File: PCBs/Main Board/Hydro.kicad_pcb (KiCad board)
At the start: 2 copper layers, 34 parts, among them J1 S2P-VHLFSN, J2 S2P-VHLFSN, J3 S2P-VHLFSN, J4 S2P-VHLFSN, J5 S2P-VHLFSN, J6 436500301, J7 436500301, J8 43650-0401, J9 S2P-VHLFSN, Q1 FQP30N06L, Q2 FQP30N06L, Q3 FQP30N06L, Q4 FQP30N06L, Q5 FQP30N06L, SW1 1825910-6, U1 19p_Header, U2 ESP32_WROOM-32U, U3 19p_Header, U4 173010378

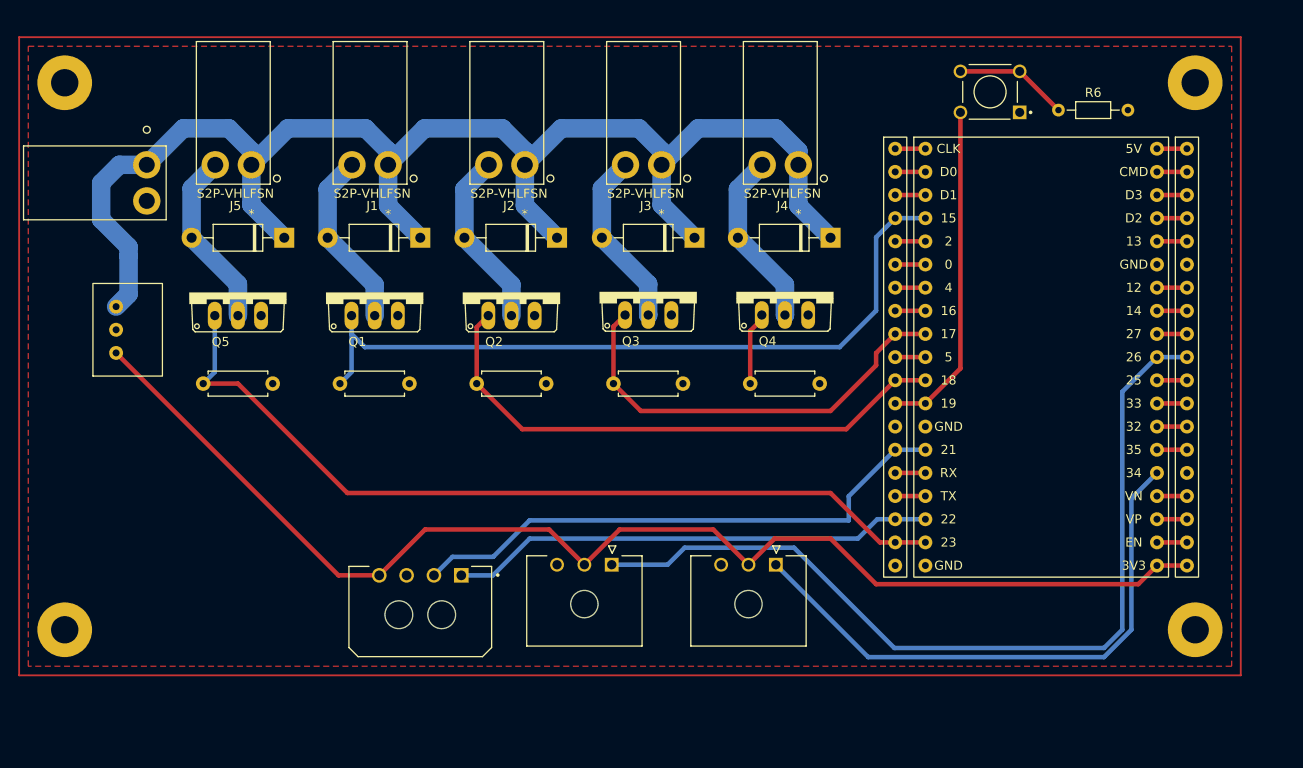
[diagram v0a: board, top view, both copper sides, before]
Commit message: Remove steppers, add OLED
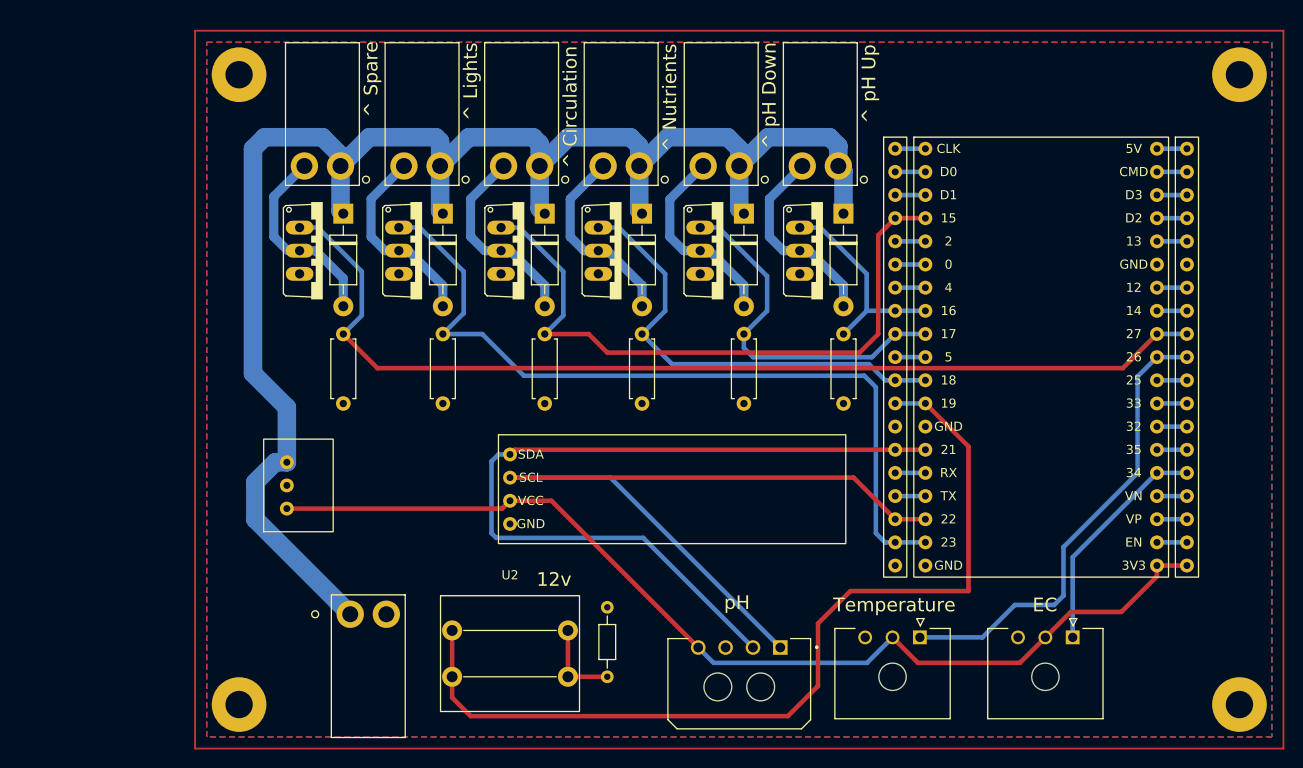
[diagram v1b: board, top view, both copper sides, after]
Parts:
- removed SW1: 1825910-6, SnapEDA Library:SW_1825910-6-4
- added D6: 1N4007, Diode_THT:D_DO-41_SOD81_P10.16mm_Horizontal, F.Cu at (130.6, 54.4)
- added J6: S2P-VHLFSN, Hydro:S2P-VHLFSN, F.Cu at (130.2, 49.1)
- added Q6: FQP30N06L, SnapEDA Library:TO220V, F.Cu at (128.3, 58.4)
- added R6: 1k, Resistor_THT:R_Axial_DIN0207_L6.3mm_D2.5mm_P7.62mm_Horizontal, F.Cu at (130.6, 67.6)
- added U2: Tactile_Button, Hydro:Tactile_Button, F.Cu at (148.8, 102.6)
- added U5: 0.91_OLED, Hydro:0.91 OLED, F.Cu at (166.6, 84.6)
- moved R7 79.5 mm to (159.5, 105.2), turned to 90 degrees
- moved J10 54.1 mm to (131.3, 98.3), turned to 0 degrees
- moved J9 35.9 mm to (174.0, 105.9)
- moved J8 34.7 mm to (193.8, 100.8)
- moved J7 33.5 mm to (210.6, 100.8)
- moved R5 26.8 mm to (141.5, 67.6), turned to -90 degrees
- moved U6 25.3 mm to (129.4, 79.1)
- moved R1 23.1 mm to (152.7, 67.6), turned to -90 degrees
- moved H2 20.8 mm to (119.1, 108.2)
- moved Q5 20.7 mm to (139.2, 58.4), turned to -90 degrees
- moved J5 20.7 mm to (141.2, 49.1)
- moved H3 19.1 mm to (119.1, 39.1)
- moved R2 18.9 mm to (163.3, 67.6), turned to -90 degrees
- moved D5 17.6 mm to (141.5, 54.4), turned to -90 degrees
- moved Q1 17.0 mm to (150.4, 58.4), turned to -90 degrees
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- renumbered J9 to J10, J6 to J7, J7 to J8, J8 to J9, R6 to R7, U2 to U3, U3 to U4, U4 to U6
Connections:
- net Net-(U2-Pad28) renamed Spare
- net pH_rx renamed SCL
- net pH_tx renamed SDA
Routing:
- net Spare: track 3.29 -> 112.2 mm
- net Net-(U1-Pad12): track 36.8 -> 100.4 mm
- net tempSignal: track 96.9 -> 51.4 mm
- net ec_A: track 62.8 -> 25.2 mm
- net SCL: track 53.5 -> 84.8 mm
- net SDA: track 61.2 -> 89.9 mm
- net 3V3: track 138.6 -> 113.9 mm
- net Net-(D6-Pad2): track 0.00 -> 21.7 mm
- net 12v: track 161.1 -> 178.0 mm
- net pHUp: track 11.2 -> 23.5 mm
- net Nutrients: track 61.5 -> 50.3 mm
- net Circulate: track 82.1 -> 71.6 mm
- net pHDown: track 47.8 -> 39.9 mm
- net Lights: track 94.4 -> 88.7 mm
- net Net-(D3-Pad2): track 19.7 -> 23.2 mm
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- added copper zone on B.Cu, net GND
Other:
- board text added: "12v"
- board text added: "EC"
- board text added: "Temperature"
- board text added: "^ Circulation"
- board text added: "^ Lights"
- board text added: "^ Nutrients"
- board text added: "^ Spare"
- board text added: "^ pH Down"
- board text added: "^ pH Up"
- board text added: "pH"

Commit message: update pcb
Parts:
- moved U6 0.86 mm to (129.9, 78.4)
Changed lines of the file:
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@@
+      (effects (font (size 1 1) (thickness 0.15)))
+    )
+    (fp_text user "SDA" (at -15.494 -3.81 unlocked) (layer "F.SilkS")
+      (effects (font (size 1 1) (thickness 0.15)))
+    )
+    (fp_text user "SCL" (at -15.494 -1.27 unlocked) (layer "F.SilkS")
+      (effects (font (size 1 1) (thickness 0.15)))
+    )
+    (fp_text user "GND" (at -15.494 3.81 unlocked) (layer "F.SilkS")
       (effects (font (size 1 1) (thickness 0.15)))
     )
@@
       (effects (font (size 1 1) (thickness 0.15)))
     )
-    (fp_text user "SCL" (at -15.494 -1.27 unlocked) (layer "F.SilkS")
-      (effects (font (size 1 1) (thickness 0.15)))
-    )
-    (fp_text user "GND" (at -15.494 3.81 unlocked) (layer "F.SilkS")
-      (effects (font (size 1 1) (thickness 0.15)))
-    )
-    (fp_text user "SDA" (at -15.494 -3.81 unlocked) (layer "F.SilkS")
-      (effects (font (size 1 1) (thickness 0.15)))
-    )
     (fp_text user "${REFERENCE}" (at 0 -7.62 unlocked) (layer "F.Fab") hide
       (effects (font (size 1 1) (thickness 0.15)))
     )
     (fp_rect (start -19.05 -5.969) (end 19.05 5.969) (layer "F.SilkS") (width 0.12) (fill none))
-    (pad "1" thru_hole circle (at -17.78 -3.81) (size 1.524 1.524) (drill 0.762) (layers *.Cu *.Mask)
+    (pad "1" thru_hole circle (at -17.78 -3.81) (size 2 2) (drill 0.9) (layers *.Cu *.Mask)
       (net 29 "SDA") (pinfunction "SDA") (pintype "input"))
-    (pad "2" thru_hole circle (at -17.78 -1.27) (size 1.524 1.524) (drill 0.762) (layers *.Cu *.Mask)
+    (pad "2" thru_hole circle (at -17.78 -1.27) (size 2 2) (drill 0.9) (layers *.Cu *.Mask)
       (net 28 "SCL") (pinfunction "SCL") (pintype "input"))
-    (pad "3" thru_hole circle (at -17.78 1.27) (size 1.524 1.524) (drill 0.762) (layers *.Cu *.Mask)
+    (pad "3" thru_hole circle (at -17.78 1.27) (size 2 2) (drill 0.9) (layers *.Cu *.Mask)
       (net 23 "3V3") (pinfunction "VCC") (pintype "input"))
-    (pad "4" thru_hole circle (at -17.78 3.81) (size 1.524 1.524) (drill 0.762) (layers *.Cu *.Mask)
+    (pad "4" thru_hole circle (at -17.78 3.81) (size 2 2) (drill 0.9) (layers *.Cu *.Mask)
       (net 7 "GND") (pinfunction "GND") (pintype "input"))
   )
   (footprint "Hydro:173010378" (layer "F.Cu")
-    (at 129.445 79.089 -90)
+    (at 129.918 78.369 -90)
     (property "Sheetfile" "File: PowerSupply.kicad_sch")
     (property "Sheetname" "Power Supply")
@@
       (effects (font (size 1 1) (thickness 0.15)))
     )
-    (fp_rect (start 10.16 7.62) (end 0 0) (layer "F.SilkS") (width 0.12) (fill none))
-    (pad "1" thru_hole circle (at 2.54 5.08 90) (size 1.524 1.524) (drill 0.762) (layers *.Cu *.Mask)
+    (fp_rect (start 11.6 7.55) (end 0 0) (layer "F.SilkS") (width 0.12) (fill none))
+    (pad "1" thru_hole circle (at 3.26 5.4 90) (size 1.524 1.524) (drill 0.762) (layers *.Cu *.Mask)
       (net 1 "12v") (pinfunction "VIN") (pintype "input"))
-    (pad "2" thru_hole circle (at 5.08 5.08 90) (size 1.524 1.524) (drill 0.762) (layers *.Cu *.Mask)
+    (pad "2" thru_hole circle (at 5.8 5.4 90) (size 1.524 1.524) (drill 0.762) (layers *.Cu *.Mask)
       (net 7 "GND") (pinfunction "GND") (pintype "output"))
-    (pad "3" thru_hole circle (at 7.62 5.08 90) (size 1.524 1.524) (drill 0.762) (layers *.Cu *.Mask)
+    (pad "3" thru_hole circle (at 8.34 5.4 90) (size 1.524 1.524) (drill 0.762) (layers *.Cu *.Mask)
       (net 23 "3V3") (pinfunction "3v3") (pintype "output"))
   )
@@
   (segment (start 183.896 45.974) (end 177.146201 45.974) (width 2.03) (layer "B.Cu") (net 1))
   (segment (start 163.015151 49.1302) (end 163.015151 54.049151) (width 2.03) (layer "B.Cu") (net 1))
-  (segment (start 121.92 45.974) (end 128.27 45.974) (width 2.03) (layer "B.Cu") (net 1))
+  (segment (start 120.65 47.244) (end 121.92 45.974) (width 2.03) (layer "B.Cu") (net 1))
   (segment (start 144.327351 45.974) (end 141.171151 49.1302) (width 2.03) (layer "B.Cu") (net 1))
+  (segment (start 123.095 81.629) (end 124.518 81.629) (width 2.03) (layer "B.Cu") (net 1))
   (segment (start 152.093151 46.683151) (end 151.384 45.974) (width 2.03) (layer "B.Cu") (net 1))
+  (segment (start 128.27 45.974) (end 130.249151 47.953151) (width 2.03) (layer "B.Cu") (net 1))
   (segment (start 120.904 87.884001) (end 131.317999 98.298) (width 2.03) (layer "B.Cu") (net 1))
   (segment (start 173.990001 49.1302) (end 173.990001 53.848001) (width 2.03) (layer "B.Cu") (net 1))
-  (segment (start 124.365 81.629) (end 124.365 75.597) (width 2.03) (layer "B.Cu") (net 1))
+  (segment (start 124.518 81.629) (end 124.518 75.75) (width 2.03) (layer "B.Cu") (net 1))
   (segment (start 130.249151 54.049151) (end 130.556 54.356) (width 2.03) (layer "B.Cu") (net 1))
   (segment (start 151.384 45.974) (end 144.327351 45.974) (width 2.03) (layer "B.Cu") (net 1))
-  (segment (start 124.365 81.629) (end 123.095 81.629) (width 2.03) (layer "B.Cu") (net 1))
+  (segment (start 120.904 83.82) (end 123.095 81.629) (width 2.03) (layer "B.Cu") (net 1))
   (segment (start 155.249351 45.974) (end 152.093151 49.1302) (width 2.03) (layer "B.Cu") (net 1))
   (segment (start 141.171151 49.1302) (end 141.171151 46.429151) (width 2.03) (layer "B.Cu") (net 1))
@@
   (segment (start 166.171351 45.974) (end 163.015151 49.1302) (width 2.03) (layer "B.Cu") (net 1))
   (segment (start 184.859151 49.1302) (end 184.859151 46.937151) (width 2.03) (layer "B.Cu") (net 1))
-  (segment (start 124.365 75.597) (end 120.65 71.882) (width 2.03) (layer "B.Cu") (net 1))
-  (segment (start 128.27 45.974) (end 130.249151 47.953151) (width 2.03) (layer "B.Cu") (net 1))
   (segment (start 152.093151 49.1302) (end 152.093151 46.683151) (width 2.03) (layer "B.Cu") (net 1))
   (segment (start 152.093151 53.795151) (end 152.654 54.356) (width 2.03) (layer "B.Cu") (net 1))
-  (segment (start 123.095 81.629) (end 120.904 83.82) (width 2.03) (layer "B.Cu") (net 1))
   (segment (start 152.093151 49.1302) (end 152.093151 53.795151) (width 2.03) (layer "B.Cu") (net 1))
-  (segment (start 120.65 47.244) (end 121.92 45.974) (width 2.03) (layer "B.Cu") (net 1))
   (segment (start 163.015151 54.049151) (end 163.322 54.356) (width 2.03) (layer "B.Cu") (net 1))
+  (segment (start 120.65 71.882) (end 120.65 47.244) (width 2.03) (layer "B.Cu") (net 1))
   (segment (start 140.716 45.974) (end 133.405351 45.974) (width 2.03) (layer "B.Cu") (net 1))
   (segment (start 173.990001 49.1302) (end 173.990001 47.244001) (width 2.03) (layer "B.Cu") (net 1))
   (segment (start 172.72 45.974) (end 166.171351 45.974) (width 2.03) (layer "B.Cu") (net 1))
-  (segment (start 120.65 71.882) (end 120.65 47.244) (width 2.03) (layer "B.Cu") (net 1))
   (segment (start 185.42 54.356) (end 185.42 49.691049) (width 2.03) (layer "B.Cu") (net 1))
-  (segment (start 130.249151 47.953151) (end 130.249151 49.1302) (width 2.03) (layer "B.Cu") (net 1))
+  (segment (start 121.92 45.974) (end 128.27 45.974) (width 2.03) (layer "B.Cu") (net 1))
   (segment (start 120.904 83.82) (end 120.904 87.884001) (width 2.03) (layer "B.Cu") (net 1))
   (segment (start 141.171151 49.1302) (end 141.171151 54.049151) (width 2.03) (layer "B.Cu") (net 1))
   (segment (start 173.990001 47.244001) (end 172.72 45.974) (width 2.03) (layer "B.Cu") (net 1))
   (segment (start 141.171151 46.429151) (end 140.716 45.974) (width 2.03) (layer "B.Cu") (net 1))
+  (segment (start 124.518 75.75) (end 120.65 71.882) (width 2.03) (layer "B.Cu") (net 1))
   (segment (start 173.990001 53.848001) (end 174.498 54.356) (width 2.03) (layer "B.Cu") (net 1))
   (segment (start 163.015151 49.1302) (end 163.015151 46.937151) (width 2.03) (layer "B.Cu") (net 1))
   (segment (start 163.015151 46.937151) (end 162.052 45.974) (width 2.03) (layer "B.Cu") (net 1))
+  (segment (start 130.249151 47.953151) (end 130.249151 49.1302) (width 2.03) (layer "B.Cu") (net 1))
   (segment (start 144.526 56.896) (end 144.526 52.737349) (width 1) (layer "B.Cu") (net 2))
   (segment (start 148.86175 58.42322) (end 147.86175 58.42322) (width 1) (layer "B.Cu") (net 2))
@@
   (segment (start 210.566 92.034) (end 219.805 82.795) (width 0.5) (layer "B.Cu") (net 22))
   (segment (start 148.844 85.852) (end 153.394 85.852) (width 0.5) (layer "F.Cu") (net 23))
-  (segment (start 147.987 86.709) (end 148.844 85.852) (width 0.5) (layer "F.Cu") (net 23))
   (segment (start 204.772 103.632) (end 207.566 100.838) (width 0.5) (layer "F.Cu") (net 23))
   (segment (start 193.596 103.632) (end 204.772 103.632) (width 0.5) (layer "F.Cu") (net 23))
   (segment (start 210.36 98.044) (end 215.9 98.044) (width 0.5) (layer "F.Cu") (net 23))
   (segment (start 219.805 92.955) (end 223.095 92.955) (width 0.5) (layer "F.Cu") (net 23))
-  (segment (start 124.365 86.709) (end 147.987 86.709) (width 0.5) (layer "F.Cu") (net 23))
   (segment (start 207.566 100.838) (end 210.36 98.044) (width 0.5) (layer "F.Cu") (net 23))
   (segment (start 190.802 100.838) (end 193.596 103.632) (width 0.5) (layer "F.Cu") (net 23))
   (segment (start 219.805 94.139) (end 219.805 92.955) (width 0.5) (layer "F.Cu") (net 23))
   (segment (start 215.9 98.044) (end 219.805 94.139) (width 0.5) (layer "F.Cu") (net 23))
+  (segment (start 124.518 86.709) (end 147.987 86.709) (width 0.5) (layer "F.Cu") (net 23))
+  (segment (start 147.987 86.709) (end 148.844 85.852) (width 0.5) (layer "F.Cu") (net 23))
   (segment (start 153.394 85.852) (end 169.49 101.948) (width 0.5) (layer "F.Cu") (net 23))
   (segment (start 171.174 103.632) (end 188.008 103.632) (width 0.5) (layer "B.Cu") (net 23))

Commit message: Finished PCBs
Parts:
- J10: value S2P-VHLFSN -> CONN_S2P-VH_JST

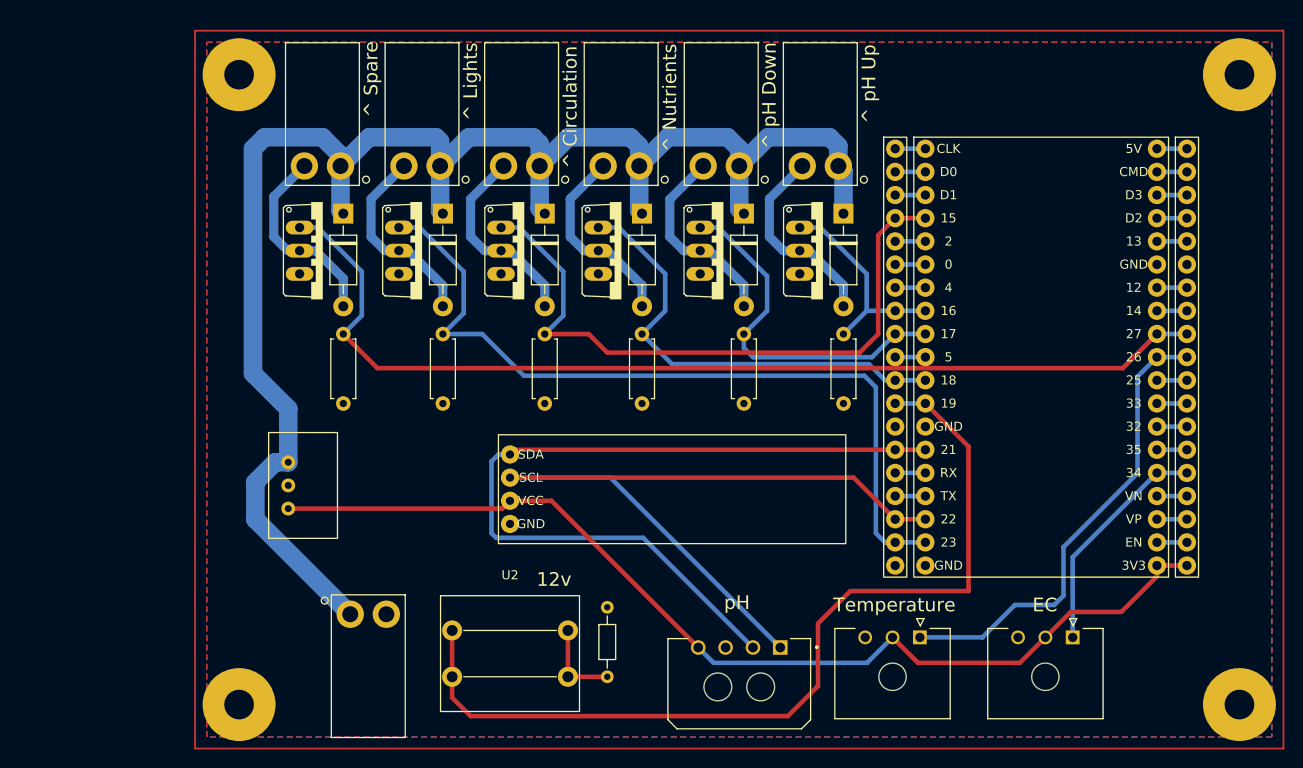
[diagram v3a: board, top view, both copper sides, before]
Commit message: Changed some pins
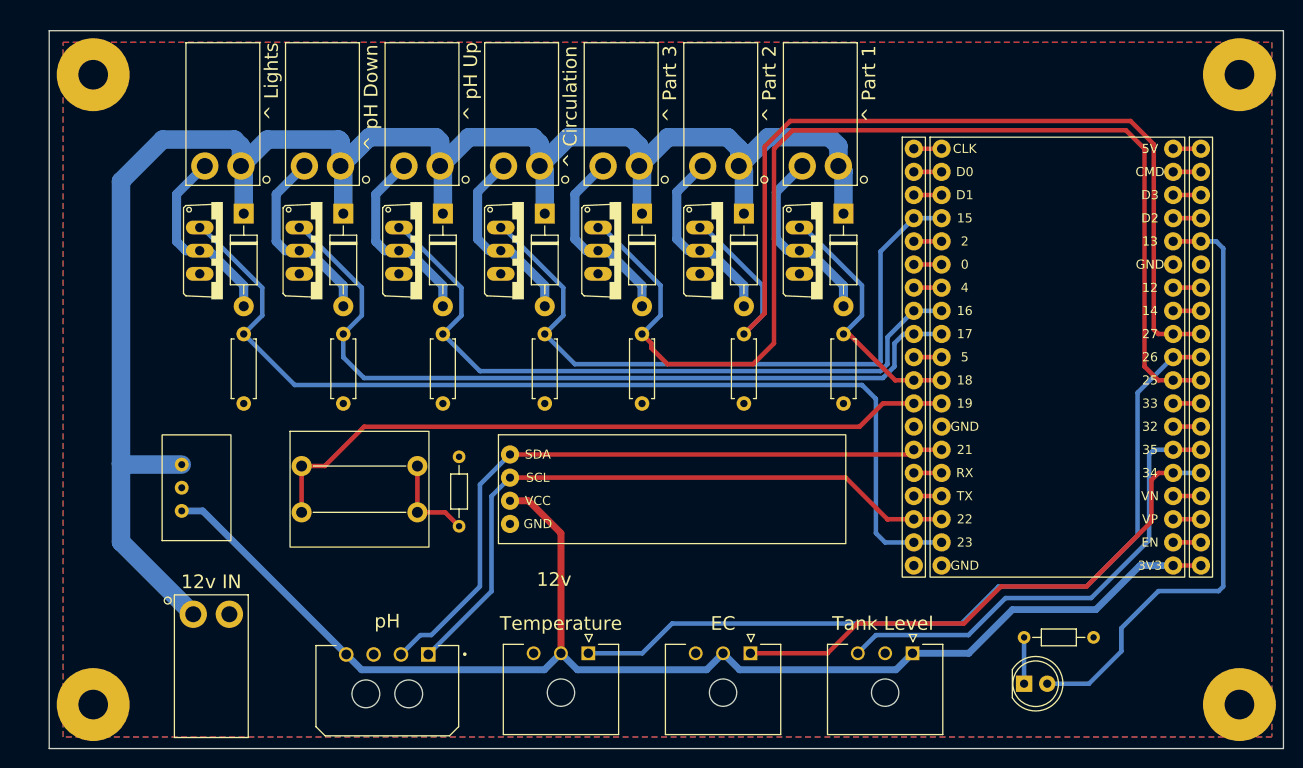
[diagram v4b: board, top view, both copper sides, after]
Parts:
- added D7: 1N4007, Diode_THT:D_DO-41_SOD81_P10.16mm_Horizontal, F.Cu at (163.3, 54.4)
- added D8: LED, LED_THT:LED_D5.0mm, F.Cu at (205.2, 105.9)
- added J11: 436500301, SnapEDA Library:MOLEX_436500301, F.Cu at (193.0, 102.6)
- added J7: S2P-VHLFSN, Hydro:S2P-VHLFSN, F.Cu at (163.0, 49.1)
- added Q7: FQP30N06L, SnapEDA Library:TO220V, F.Cu at (161.0, 58.4)
- added R7: 1k, Resistor_THT:R_Axial_DIN0207_L6.3mm_D2.5mm_P7.62mm_Horizontal, F.Cu at (163.3, 67.6)
- added R9: R_Small_US, Resistor_THT:R_Axial_DIN0204_L3.6mm_D1.6mm_P7.62mm_Horizontal, F.Cu at (205.2, 100.8)
- J12: renamed from J10; value CONN_S2P-VH_JST -> S2P-VHLFSN
- moved Q3 44.0 mm to (128.3, 58.4)
- moved Q4 44.0 mm to (139.2, 58.4)
- moved D3 43.9 mm to (130.6, 54.4)
- moved D4 43.9 mm to (141.5, 54.4)
- moved D6 43.9 mm to (174.5, 54.4)
- moved R3 43.9 mm to (130.6, 67.6)
- moved R4 43.9 mm to (141.5, 67.6)
- moved R6 43.9 mm to (174.5, 67.6)
- moved Q6 43.9 mm to (172.2, 58.4)
- moved J3 43.7 mm to (130.2, 49.1)
- moved J6 43.7 mm to (173.9, 49.1)
- moved J4 43.7 mm to (141.2, 49.1)
- moved J10 38.6 mm to (135.4, 106.7)
- moved J9 36.4 mm to (157.4, 102.6)
- moved J8 35.4 mm to (175.2, 102.6)
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- renumbered J9 to J10, J7 to J8, J8 to J9, R7 to R8
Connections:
- net Net-(U3-Pad30) renamed Part3
- net Net-(U3-Pad33) renamed waterLevel
- net Nutrients renamed Part1
- net Spare renamed Part2
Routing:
- net Part3: track 3.29 -> 127.1 mm
- net Net-(U3-Pad24): track 3.29 -> 68.1 mm
- net pHUp: track 23.5 -> 76.4 mm
- net waterLevel: track 3.29 -> 52.4 mm
- net pHDown: track 39.9 -> 88.1 mm
- net tempSignal: track 51.4 -> 89.8 mm
- net ec_A: track 25.2 -> 60.3 mm
- net 3V3: track 113.7 -> 147.0 mm
- net 12v: track 178.2 -> 202.1 mm
- net Net-(D7-Pad2): track 0.00 -> 23.4 mm
- net Net-(U1-Pad12): track 100.4 -> 78.1 mm
- net Part1: track 50.3 -> 28.5 mm
- net Lights: track 88.7 -> 110.2 mm
- net SDA: track 89.9 -> 75.1 mm
- net SCL: track 84.8 -> 72.3 mm
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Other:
- board outline added: 135.4 x 78.7 mm
- board text added: "12v IN"
- board text added: "Tank Level"
- board text added: "^ Part 1"
- board text added: "^ Part 2"
- board text added: "^ Part 3"
- board text removed: "^ Nutrients"
- board text removed: "^ Spare"
